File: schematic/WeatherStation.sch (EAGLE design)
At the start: 22 parts, among them Q1 BS250, Q2 BS250

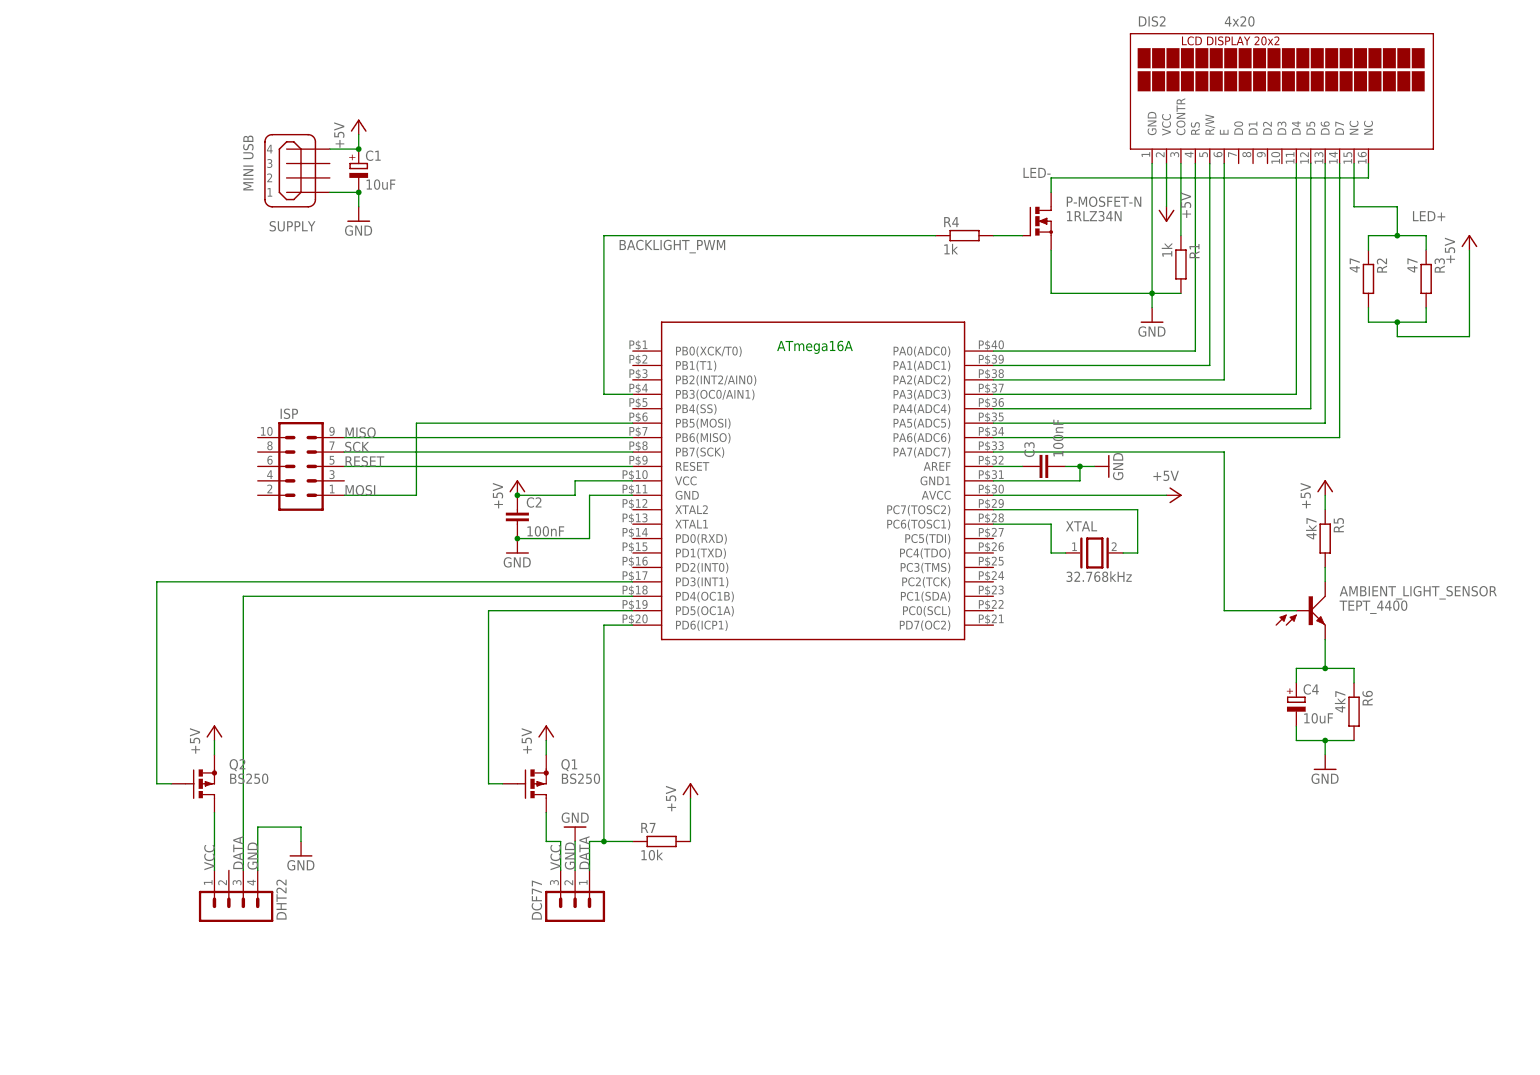
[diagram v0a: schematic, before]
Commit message: Updated schematic, only formal modifications.
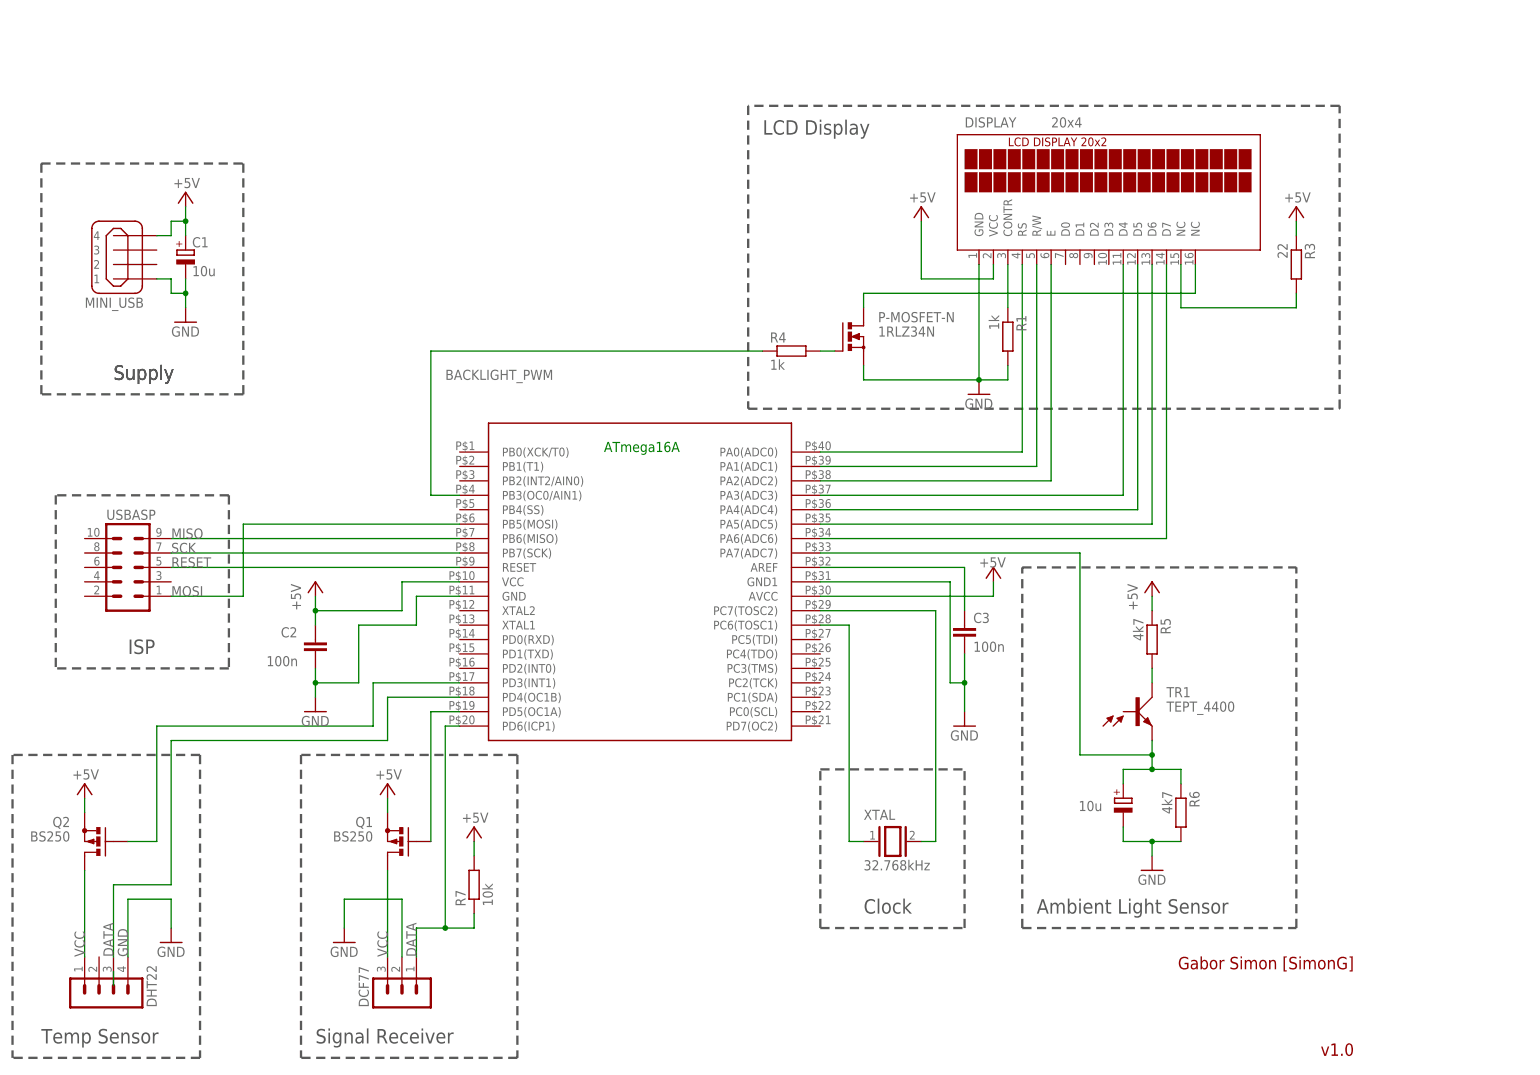
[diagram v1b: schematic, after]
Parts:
- removed AMBIENT_LIGHT_SENSOR: TEPT_4400, opto-trans-siemens:BP103
- removed DIS2: 4x20, display-lcd:TUXGR_20X2
- removed ISP: (no value), con-lstb:MA05-2
- removed R2: 47, rcl:R-EU_0204/7
- removed SUPPLY: MINI USB, con-cypressindustries:MINI-USB_4P-85-32004-10X
- added DISPLAY: 20x4, display-lcd:TUXGR_20X2
- added MINI_USB: MINI USB, con-cypressindustries:MINI-USB_4P-85-32004-10X
- added TR1: TEPT_4400, opto-trans-siemens:BP103
- added USBASP: (no value), con-lstb:MA05-2
- C1, C4: value 10uF -> 10u
- C2, C3: value 100nF -> 100n
- R3: value 47 -> 22
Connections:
- removed net N$25: AMBIENT_LIGHT_SENSOR.E, C4.+, R6.1
- net +5V: now also DISPLAY.VCC, MINI_USB.4, R3.1; no longer DIS2.VCC, R2.2, R3.2, SUPPLY.4
- net GND: now also DISPLAY.GND, MINI_USB.1; no longer DIS2.GND, SUPPLY.1
- net LED+: now also DISPLAY.NC@1, R3.2; no longer DIS2.NC@1, R2.1, R3.1
- net LED-: now also DISPLAY.NC@2; no longer DIS2.NC@2
- net MISO: now also USBASP.9; no longer ISP.9
- net MOSI: now also USBASP.1; no longer ISP.1
- net N$1: now also DISPLAY.E; no longer DIS2.E
- net N$12: now also C4.+, R6.1, TR1.E; no longer AMBIENT_LIGHT_SENSOR.B
- net N$18: now also TR1.C; no longer AMBIENT_LIGHT_SENSOR.C
- net N$2: now also DISPLAY.R/W; no longer DIS2.R/W
- net N$21: now also DISPLAY.CONTR; no longer DIS2.CONTR
- net N$3: now also DISPLAY.RS; no longer DIS2.RS
- net N$4: now also DISPLAY.D7; no longer DIS2.D7
- net N$5: now also DISPLAY.D6; no longer DIS2.D6
- net N$6: now also DISPLAY.D5; no longer DIS2.D5
- net N$7: now also DISPLAY.D4; no longer DIS2.D4
- net RESET: now also USBASP.5; no longer ISP.5
- net SCK: now also ATMEGA_16A.PB7(SCK), USBASP.7; no longer ISP.7
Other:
- note added: "Ambient Light Sensor"
- note added: "Clock"
- note added: "Gabor Simon [SimonG]"
- note added: "ISP"
- note added: "LCD Display"
- note added: "Signal Receiver"
- note added: "Supply"
- note added: "Temp Sensor"
- note added: "v1.0"
- moved on the sheet: C1, C2, C3, DCF77, DHT22, P-MOSFET-N, Q1, Q2, R1, R3, R4, R5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
